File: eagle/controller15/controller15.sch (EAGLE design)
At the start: 68 parts, among them IC1 MCP170312MB, IC3 FE1.1S, Q1 FDD4141TO252, Q2 200mA/50V, Q3 FDD4141TO252, Q4 200mA/50V, Q5 FDD4141TO252, Q6 200mA/50V, Q7 FDD4141TO252, Q8 200mA/50V, U1 ATSAMD21G-A, U3 MP2307, Y2 32.768

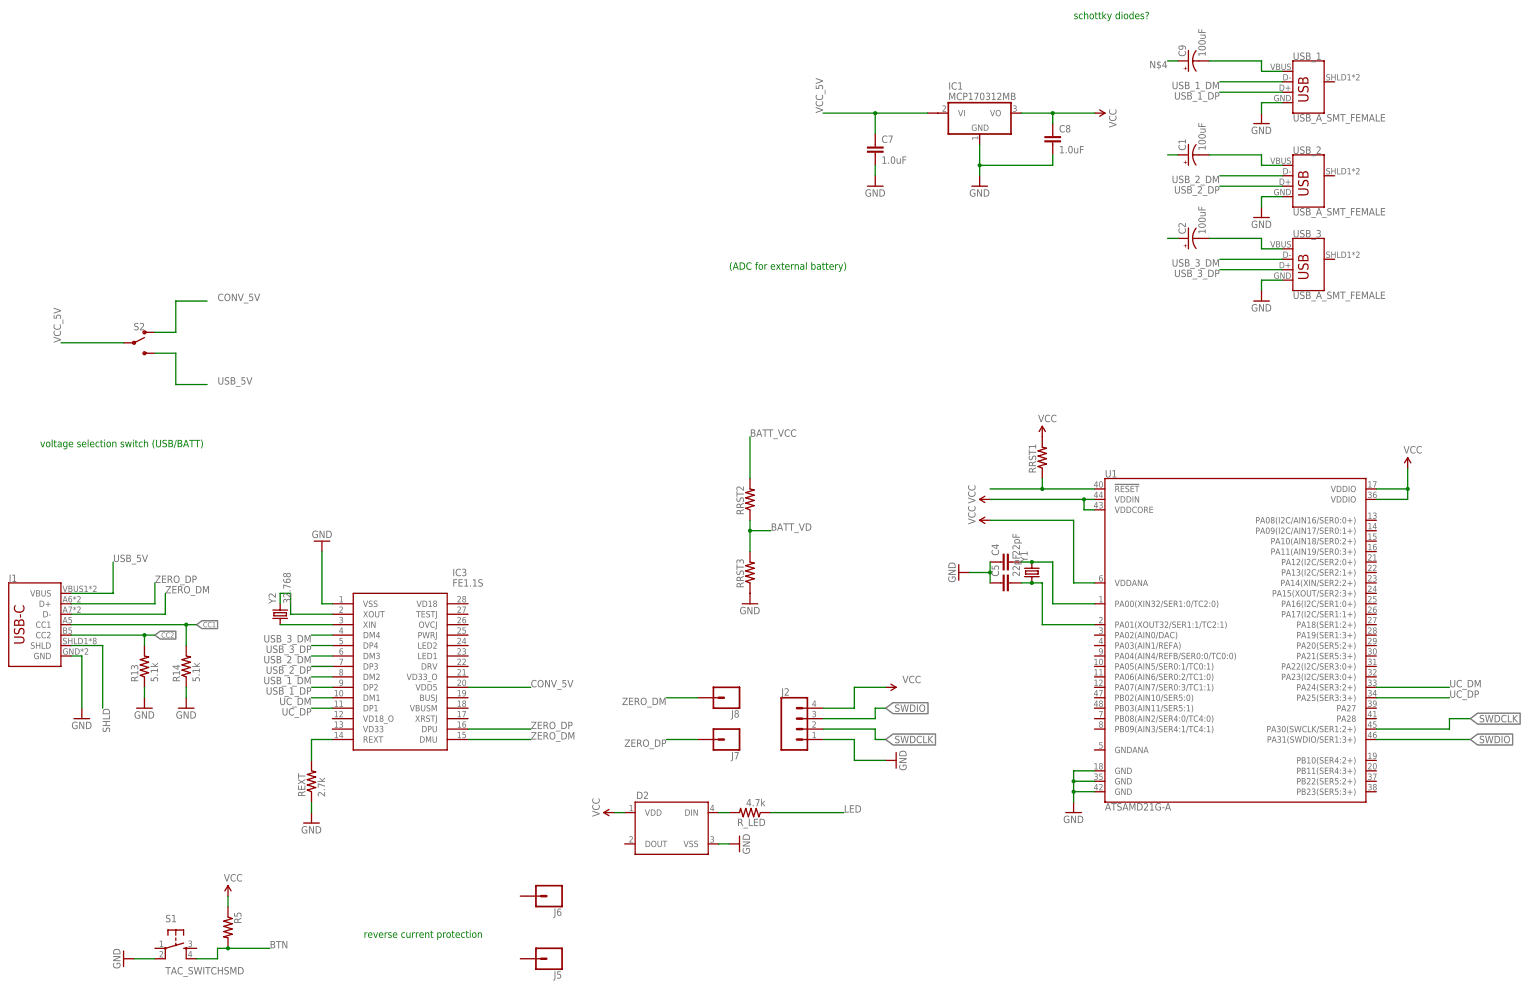
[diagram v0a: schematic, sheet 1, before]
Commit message: controller15 board files nearly finished usbDirectController3 firmware
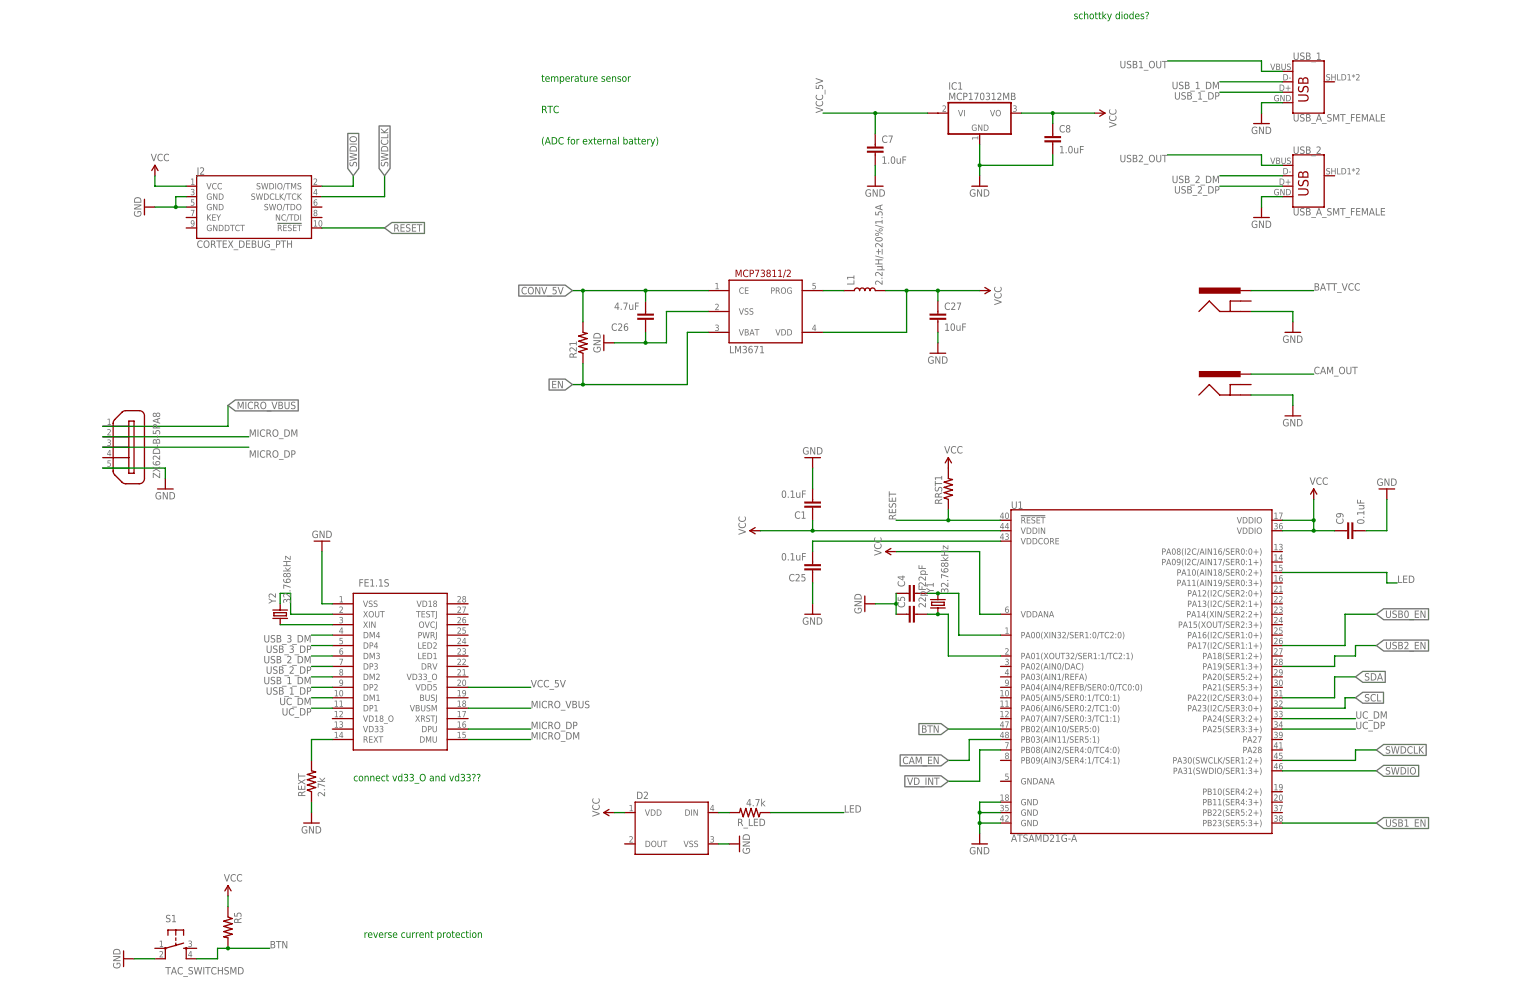
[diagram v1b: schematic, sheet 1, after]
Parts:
- removed J1: (no value), SparkFun-Connectors:USB_C16PIN
- removed J5, J6, J7, J8: (no value), SparkFun-Connectors:CONN_01POGOPIN_HOLE_0.58
- removed Q1, Q5, Q7: FDD4141TO252, transistor-fet:FDD4141TO252
- removed Q2, Q6, Q8: 200mA/50V, SparkFun-DiscreteSemi:MOSFET-NCHANNELBSS138
- removed R10, R12, R8: 1k, SparkFun-Resistors:RESISTOR1206
- removed R11, R7, R9: 10k, SparkFun-Resistors:RESISTOR1206
- removed R13, R14: 5.1k, SparkFun-Passives:RESISTOR1206
- removed RRST2, RRST3: (no value), SparkFun-Passives:RESISTOR1206
- removed S2: (no value), SparkFun-Switches:SWITCH-SPDT-SMD-RIGHT-ANGLE
- removed U$4: NANOFIT2, volzolib:NANOFIT2
- removed USB_3: USB_A_SMT_FEMALE, SparkFun-Connectors:USB_A_SMT_FEMALE
- added AP1, AP2, AP2553: MCP4725, SparkFun-IC-Conversion:MCP4725SOT-23
- added C10, C21, C27, C3: 10uF, SparkFun-Capacitors:1.0UF-1206-50V-10%
- added C11, C17, C22, C25: 0.1uF, SparkFun-Capacitors:1.0UF-0805-25V-10%
- added C12, C18, C23: 1.0uF, SparkFun-Capacitors:1.0UF-1206-50V-10%
- added C20, C24: 120uF, SparkFun-Capacitors:1.0UF-1206-50V-10%
- added C26: 4.7uF, SparkFun-Capacitors:1.0UF-1206-50V-10%
- added D1: 3A/40V/500mV, SparkFun-DiscreteSemi:DIODE-SCHOTTKY-B340A
- added J3, J4: POWER_JACKPTH_BREAD, SparkFun-Connectors:POWER_JACKPTH_BREAD
- added L1: 2.2µH/±20%/1.5A, SparkFun-Coils:INDUCTOR-VLF4012AT-2.2UH
- added LM3671: MCP73811/2, adafruit:MCP73811/2
- added MCP9808: V_REG_MIC5216, SparkFun-IC-Power:V_REG_MIC5216
- added R21: (no value), SparkFun-Passives:RESISTOR0805-RES
- added R_I2C_1, R_I2C_2, R_MOSFET_USB3, R_MOSFET_USB4, R_MOSFET_USB6: 10k, SparkFun-Passives:RESISTOR0805-RES
- added R_MOSFET_USB1, R_MOSFET_USB2, R_MOSFET_USB5: ? (1%), SparkFun-Passives:RESISTOR0805-RES
- added X2: ZX62D-B-5PA8, zx62d-b-5pa8-oshpark_10:ZX62D-B-5PA8
- C1, C9: value 100uF -> 0.1uF; device SparkFun-Capacitors:100UF-POLAR-25V-20%(ELEC) -> SparkFun-Capacitors:1.0UF-0805-25V-10%
- C13: device SparkFun-Capacitors:CAP1206 -> SparkFun-Capacitors:CAP0805
- C2: value 100uF -> 120uF; device SparkFun-Capacitors:100UF-POLAR-25V-20%(ELEC) -> SparkFun-Capacitors:1.0UF-1206-50V-10%
- C4, C5: device SparkFun-Passives:CAP1206 -> SparkFun-Passives:CAP0805
- J2: value (none) -> CORTEX_DEBUG_PTH; device SparkFun-Connectors:CONN_04 -> SparkFun-Connectors:CORTEX_DEBUG_PTH
- R2, R24: device SparkFun-Resistors:RESISTOR0805-RES -> SparkFun-Resistors:RESISTOR1206
- R4, R6, R_LED: device SparkFun-Resistors:RESISTOR1206 -> SparkFun-Resistors:RESISTOR0805-RES
- R5, REXT, RRST1: device SparkFun-Passives:RESISTOR1206 -> SparkFun-Passives:RESISTOR0805-RES
- S1: device SparkFun-Retired:TAC_SWITCHPTH -> SparkFun-Retired:TAC_SWITCHSMD
- Y1: value (none) -> 32.768kHz; device SparkFun-FreqCtrl:CRYSTALCRYSTAL-SMD-5X3-16MHZ -> SparkFun-FreqCtrl:CRYSTAL3.2X1.5MM
- Y2: value 32.768 -> 32.768kHz; device SparkFun-FreqCtrl:CRYSTALCRYSTAL-SMD-5X3-16MHZ -> SparkFun-FreqCtrl:CRYSTAL3.2X1.5MM
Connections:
- removed net BATT_VD: RRST2.1, RRST3.2
- removed net CC1: J1.CC1, R14.2
- removed net CC2: J1.CC2, R13.2
- removed net HUB_1: Q3.D
- removed net HUB_1_EN: R6.1
- removed net HUB_2: Q1.D
- removed net HUB_2_EN: R10.1
- removed net HUB_3: Q5.D
- removed net HUB_3_EN: R8.1
- removed net HUB_ZERO: Q7.D
- removed net HUB_ZERO_EN: R12.1
- removed net N$12: Q5.G, Q6.D, R7.2
- removed net N$13: Q6.G, R8.2
- removed net N$15: Q7.G, Q8.D, R11.2
- removed net N$19: Q8.G, R12.2
- removed net N$21: RRST1.1, U1.!RESET!
- removed net N$34: C1.-, USB_2.VBUS
- removed net N$35: C9.-, USB_1.VBUS
- removed net N$40: C2.-, USB_3.VBUS
- removed net N$6: Q2.G, R10.2
- removed net SHLD: J1.SHLD
- removed net USB_5V: J1.VBUS, S2.S
- removed net ZERO_DM: IC3.DMU, J1.D-, J8.1
- removed net ZERO_DP: IC3.DPU, J1.D+, J7.1
- new net CAM_EN: R6.1, U1.PB03(AIN11/SER5:1)
- new net CAM_OUT: J3.PWR, Q3.D
- new net EN: LM3671.VBAT, R21.1
- new net MICRO_DM: IC3.DMU, X2G$1.2
- new net MICRO_DP: IC3.DPU, X2G$1.3
- new net MICRO_VBUS: AP2.AO, C23.2, C24.2, IC3.VBUSM, X2G$1.1
- new net N$10: AP1.SCL, R_MOSFET_USB2.2
- new net N$11: AP2.SCL, R_MOSFET_USB5.2
- new net RESET: J2.!RESET, RRST1.1, U1.!RESET!
- new net SCL: MCP9808.VIN, R_I2C_1.2, U1.PA23(I2C/SER3:0+)
- new net SDA: MCP9808.EN, R_I2C_2.1, U1.PA22(I2C/SER3:0+)
- new net USB0_EN: AP2.VDD, R_MOSFET_USB6.2, U1.PA17(I2C/SER1:1+)
- new net USB1_EN: AP2553.VDD, R_MOSFET_USB3.2, U1.PB23(SER5:3+)
- new net USB1_OUT: AP2553.AO, C12.2, C2.2, USB_1.VBUS
- new net USB2_EN: AP1.VDD, R_MOSFET_USB4.2, U1.PA19(SER1:3+)
- new net USB2_OUT: AP1.AO, C18.2, C20.2, USB_2.VBUS
- net BATT_VCC: now also J4.PWR, Q3.S, R4.1; no longer RRST2.2, U$4.LEFT
- net BTN: now also U1.PB02(AIN10/SER5:0)
- net CONV_5V: now also C26.2, LM3671.CE, R21.2; no longer IC3.VDD5, S2.O
- net GND: now also AP1.VSS, AP2.VSS, AP2553.VSS, C1.2, C10.2, C11.2, C12.1, C17.2, C18.1, C2.1, C20.1, C21.2, C22.2, C23.1, C24.1, C25.1, C26.1, C27.2, C3.2, C9.2, J2.GND@3, J2.GND@5, J3.GND, J4.GND, LM3671.VSS, MCP9808.FLAG, MCP9808.GND@5, MCP9808.GND@6, MCP9808.GND@7, R_MOSFET_USB1.1, R_MOSFET_USB2.1, R_MOSFET_USB3.1, R_MOSFET_USB4.1, R_MOSFET_USB5.1, R_MOSFET_USB6.1, X2G$1.5; no longer J1.GND, J2.1, Q2.S, Q6.S, Q8.S, R13.1, R14.1, RRST3.1, U$4.RIGHT, USB_3.GND
- net GNDA: now also D1.A
- net LED: now also U1.PA10(AIN18/SER0:2+)
- net N$1: now also L1.1, LM3671.PROG; no longer Q1.G, Q2.D, R9.2
- net N$26: now also D1.C
- net N$4: now also MCP9808.VOUT; no longer C9.+
- net N$5: now also C25.2, U1.VDDCORE; no longer C1.+
- net N$9: now also AP2553.SCL, R_MOSFET_USB1.2; no longer C2.+
- net SWDCLK: now also J2.SWDCLK/TCK; no longer J2.2
- net SWDIO: now also J2.SWDIO/TMS; no longer J2.3
- net USB_3_DM: no longer USB_3.D-
- net USB_3_DP: no longer USB_3.D+
- net VCC: now also C1.1, C27.1, C9.1, J2.VCC, L1.2, LM3671.VDD, MCP9808.GND@8, R_I2C_1.1, R_I2C_2.2; no longer J2.4, U1.VDDCORE
- net VCC_5V: now also AP1.VOUT, AP2.VOUT, AP2553.VOUT, C10.1, C11.1, C17.1, C21.1, C22.1, C3.1, IC3.VDD5; no longer Q1.S, Q3.S, Q5.S, Q7.S, R11.1, R4.1, R7.1, R9.1, S2.P
- net VD_INT: now also U1.PB08(AIN2/SER4:0/TC4:0)
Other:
- note added: "AP2553"
- note added: "RTC"
- note added: "connect vd33_O and vd33??"
- note added: "temperature sensor"
- note removed: "voltage selection switch (USB/BATT)"
- moved on the sheet: C4, C5, H1, H2, H3, H4, L2, RRST1, SH2, U1, Y1

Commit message: minor changes
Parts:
- C25: value 0.1uF -> 1.0uF
- R_LED: value 4.7k -> 470
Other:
- note added: "correct crystal??"
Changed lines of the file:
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@@
 <grid distance="0.1" unitdist="inch" unit="inch" style="lines" multiple="1" display="no" altdistance="0.01" altunitdist="inch" altunit="inch"/>
 <layers>
-<layer number="1" name="Top" color="4" fill="1" visible="yes" active="no"/>
-<layer number="2" name="Route2" color="1" fill="3" visible="yes" active="no"/>
-<layer number="3" name="Route3" color="4" fill="3" visible="yes" active="no"/>
-<layer number="4" name="Route4" color="1" fill="4" visible="yes" active="no"/>
-<layer number="5" name="Route5" color="4" fill="4" visible="yes" active="no"/>
-<layer number="6" name="Route6" color="1" fill="8" visible="yes" active="no"/>
-<layer number="7" name="Route7" color="4" fill="8" visible="yes" active="no"/>
-<layer number="8" name="Route8" color="1" fill="2" visible="yes" active="no"/>
-<layer number="9" name="Route9" color="4" fill="2" visible="yes" active="no"/>
-<layer number="10" name="Route10" color="1" fill="7" visible="yes" active="no"/>
-<layer number="11" name="Route11" color="4" fill="7" visible="yes" active="no"/>
-<layer number="12" name="Route12" color="1" fill="5" visible="yes" active="no"/>
-<layer number="13" name="Route13" color="4" fill="5" visible="yes" active="no"/>
-<layer number="14" name="Route14" color="1" fill="6" visible="yes" active="no"/>
-<layer number="15" name="Route15" color="4" fill="6" visible="yes" active="no"/>
-<layer number="16" name="Bottom" color="1" fill="1" visible="yes" active="no"/>
-<layer number="17" name="Pads" color="2" fill="1" visible="yes" active="no"/>
-<layer number="18" name="Vias" color="2" fill="1" visible="yes" active="no"/>
-<layer number="19" name="Unrouted" color="6" fill="1" visible="yes" active="no"/>
-<layer number="20" name="Dimension" color="15" fill="1" visible="yes" active="no"/>
-<layer number="21" name="tPlace" color="7" fill="1" visible="yes" active="no"/>
-<layer number="22" name="bPlace" color="7" fill="1" visible="yes" active="no"/>
-<layer number="23" name="tOrigins" color="15" fill="1" visible="yes" active="no"/>
-<layer number="24" name="bOrigins" color="15" fill="1" visible="yes" active="no"/>
-<layer number="25" name="tNames" color="7" fill="1" visible="yes" active="no"/>
-<layer number="26" name="bNames" color="7" fill="1" visible="yes" active="no"/>
-<layer number="27" name="tValues" color="7" fill="1" visible="yes" active="no"/>
-<layer number="28" name="bValues" color="7" fill="1" visible="yes" active="no"/>
+<layer number="1" name="Top" color="4" fill="1" visible="no" active="no"/>
+<layer number="2" name="Route2" color="1" fill="3" visible="no" active="no"/>
+<layer number="3" name="Route3" color="4" fill="3" visible="no" active="no"/>
+<layer number="4" name="Route4" color="1" fill="4" visible="no" active="no"/>
+<layer number="5" name="Route5" color="4" fill="4" visible="no" active="no"/>
+<layer number="6" name="Route6" color="1" fill="8" visible="no" active="no"/>
+<layer number="7" name="Route7" color="4" fill="8" visible="no" active="no"/>
+<layer number="8" name="Route8" color="1" fill="2" visible="no" active="no"/>
+<layer number="9" name="Route9" color="4" fill="2" visible="no" active="no"/>
+<layer number="10" name="Route10" color="1" fill="7" visible="no" active="no"/>
+<layer number="11" name="Route11" color="4" fill="7" visible="no" active="no"/>
+<layer number="12" name="Route12" color="1" fill="5" visible="no" active="no"/>
+<layer number="13" name="Route13" color="4" fill="5" visible="no" active="no"/>
+<layer number="14" name="Route14" color="1" fill="6" visible="no" active="no"/>
+<layer number="15" name="Route15" color="4" fill="6" visible="no" active="no"/>
+<layer number="16" name="Bottom" color="1" fill="1" visible="no" active="no"/>
+<layer number="17" name="Pads" color="2" fill="1" visible="no" active="no"/>
+<layer number="18" name="Vias" color="2" fill="1" visible="no" active="no"/>
+<layer number="19" name="Unrouted" color="6" fill="1" visible="no" active="no"/>
+<layer number="20" name="Dimension" color="15" fill="1" visible="no" active="no"/>
+<layer number="21" name="tPlace" color="7" fill="1" visible="no" active="no"/>
+<layer number="22" name="bPlace" color="7" fill="1" visible="no" active="no"/>
+<layer number="23" name="tOrigins" color="15" fill="1" visible="no" active="no"/>
+<layer number="24" name="bOrigins" color="15" fill="1" visible="no" active="no"/>
+<layer number="25" name="tNames" color="7" fill="1" visible="no" active="no"/>
+<layer number="26" name="bNames" color="7" fill="1" visible="no" active="no"/>
+<layer number="27" name="tValues" color="7" fill="1" visible="no" active="no"/>
+<layer number="28" name="bValues" color="7" fill="1" visible="no" active="no"/>
 <layer number="29" name="tStop" color="7" fill="3" visible="no" active="no"/>
 <layer number="30" name="bStop" color="7" fill="6" visible="no" active="no"/>
@@
 <layer number="35" name="tGlue" color="7" fill="4" visible="no" active="no"/>
 <layer number="36" name="bGlue" color="7" fill="5" visible="no" active="no"/>
-<layer number="37" name="tTest" color="7" fill="1" visible="yes" active="no"/>
-<layer number="38" name="bTest" color="7" fill="1" visible="yes" active="no"/>
+<layer number="37" name="tTest" color="7" fill="1" visible="no" active="no"/>
+<layer number="38" name="bTest" color="7" fill="1" visible="no" active="no"/>
 <layer number="39" name="tKeepout" color="4" fill="11" visible="no" active="no"/>
 <layer number="40" name="bKeepout" color="1" fill="11" visible="no" active="no"/>
@@
 <layer number="44" name="Drills" color="7" fill="1" visible="no" active="no"/>
 <layer number="45" name="Holes" color="7" fill="1" visible="no" active="no"/>
-<layer number="46" name="Milling" color="3" fill="1" visible="yes" active="no"/>
-<layer number="47" name="Measures" color="7" fill="1" visible="yes" active="no"/>
-<layer number="48" name="Document" color="7" fill="1" visible="yes" active="no"/>
-<layer number="49" name="Reference" color="7" fill="1" visible="yes" active="no"/>
-<layer number="50" name="dxf" color="7" fill="1" visible="yes" active="no"/>
-<layer number="51" name="tDocu" color="7" fill="1" visible="yes" active="no"/>
-<layer number="52" name="bDocu" color="7" fill="1" visible="yes" active="no"/>
-<layer number="53" name="tGND_GNDA" color="7" fill="9" visible="yes" active="no"/>
-<layer number="54" name="bGND_GNDA" color="1" fill="9" visible="yes" active="no"/>
-<layer number="56" name="wert" color="7" fill="1" visible="yes" active="no"/>
-<layer number="57" name="tCAD" color="7" fill="1" visible="yes" active="no"/>
-<layer number="59" name="tCarbon" color="7" fill="1" visible="yes" active="no"/>
-<layer number="60" name="bCarbon" color="7" fill="1" visible="yes" active="no"/>
+<layer number="46" name="Milling" color="3" fill="1" visible="no" active="no"/>
+<layer number="47" name="Measures" color="7" fill="1" visible="no" active="no"/>
+<layer number="48" name="Document" color="7" fill="1" visible="no" active="no"/>
+<layer number="49" name="Reference" color="7" fill="1" visible="no" active="no"/>
+<layer number="50" name="dxf" color="7" fill="1" visible="no" active="no"/>
+<layer number="51" name="tDocu" color="7" fill="1" visible="no" active="no"/>
+<layer number="52" name="bDocu" color="7" fill="1" visible="no" active="no"/>
+<layer number="53" name="tGND_GNDA" color="7" fill="9" visible="no" active="no"/>
+<layer number="54" name="bGND_GNDA" color="1" fill="9" visible="no" active="no"/>
+<layer number="56" name="wert" color="7" fill="1" visible="no" active="no"/>
+<layer number="57" name="tCAD" color="7" fill="1" visible="no" active="no"/>
+<layer number="59" name="tCarbon" color="7" fill="1" visible="no" active="no"/>
+<layer number="60" name="bCarbon" color="7" fill="1" visible="no" active="no"/>
 <layer number="88" name="SimResults" color="9" fill="1" visible="yes" active="yes"/>
 <layer number="89" name="SimProbes" color="9" fill="1" visible="yes" active="yes"/>
@@
 <part name="GND18" library="SparkFun-Aesthetics" deviceset="GND" device=""/>
 <part name="SUPPLY12" library="SparkFun-Aesthetics" deviceset="VCC" device=""/>
-<part name="R_LED" library="SparkFun-Resistors" deviceset="RESISTOR" device="0805-RES" value="4.7k"/>
+<part name="R_LED" library="SparkFun-Resistors" deviceset="RESISTOR" device="0805-RES" value="470"/>
 <part name="FRAME2" library="frames" deviceset="DINA4_L" device=""/>
 <part name="FRAME3" library="frames" deviceset="A3L-LOC" device=""/>
@@
 <part name="SUPPLY1" library="SparkFun-Aesthetics" deviceset="VCC" device=""/>
 <part name="C1" library="SparkFun-Capacitors" library_urn="urn:adsk.eagle:library:510" deviceset="1.0UF" device="-0805-25V-10%" package3d_urn="urn:adsk.eagle:package:37429/1" value="0.1uF"/>
-<part name="C25" library="SparkFun-Capacitors" library_urn="urn:adsk.eagle:library:510" deviceset="1.0UF" device="-0805-25V-10%" package3d_urn="urn:adsk.eagle:package:37429/1" value="0.1uF"/>
+<part name="C25" library="SparkFun-Capacitors" library_urn="urn:adsk.eagle:library:510" deviceset="1.0UF" device="-0805-25V-10%" package3d_urn="urn:adsk.eagle:package:37429/1" value="1.0uF"/>
 <part name="GND16" library="SparkFun-Aesthetics" deviceset="GND" device=""/>
 <part name="GND22" library="SparkFun-Aesthetics" deviceset="GND" device=""/>
@@
 <text x="142.24" y="233.68" size="1.778" layer="91">temperature sensor</text>
 <text x="142.24" y="226.06" size="1.778" layer="91">RTC</text>
+<text x="99.06" y="119.38" size="1.778" layer="91">correct crystal??</text>
 </plain>
 <instances>
